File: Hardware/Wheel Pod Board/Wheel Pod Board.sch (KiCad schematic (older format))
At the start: 33 parts, among them J1 Conn_RJ-45, P1 UIM240XX_Stepper_Conn, P2 RS232, P3 ST_SWD_Connector, P4 SyRen, P5 BATT, U1 STM32F401RCT6, U2 SN75176BDR, U3 ZXCT1107, U4 ZXCT1107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

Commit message: Change header footprints to new ones in schematic
Forgot to save this until now, did this before I made the PCB changes
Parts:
- P1, P3: footprint MAVRIC_footprints:1x6_SMD_header -> MAVRIC_footprints:1x6_Breakaway_Header
- P2: footprint MAVRIC_footprints:1x3_SMD_header -> MAVRIC_footprints:1x3_Breakaway_Header
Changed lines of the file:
@@
 Connection ~ 6100 1400
 Wire Wire Line
-	5950 1800 6100 1800
-Wire Wire Line
-	6100 1800 6800 1800
+	5950 1800 6800 1800
 Connection ~ 6100 1800
 Wire Wire Line
@@
 Connection ~ 6600 1100
 Wire Wire Line
-	6100 1200 6100 1400
-Wire Wire Line
-	6100 1400 6100 1600
-Wire Wire Line
-	6100 1600 6100 1800
-Wire Wire Line
-	6600 1000 6600 1100
-Wire Wire Line
-	6600 1100 6600 1300
-Wire Wire Line
-	6600 1300 6600 1500
-Wire Wire Line
-	6600 1500 6600 1700
-Wire Wire Line
-	6600 1700 6600 1900
+	6100 1200 6100 1800
+Wire Wire Line
+	6600 1000 6600 1900
 Wire Wire Line
 	5950 2600 6100 2600
@@
 	2350 7100 2500 7100
 Wire Wire Line
-	1750 7000 2350 7000
-Wire Wire Line
-	2350 7000 2500 7000
+	1750 7000 2500 7000
 Wire Wire Line
 	2500 7200 2350 7200
@@
 	9900 1650 9900 1750
 Wire Wire Line
-	7500 1500 7500 1650
-Wire Wire Line
-	7500 1650 7500 1750
+	7500 1500 7500 1750
 Connection ~ 7500 1650
 Wire Wire Line
@@
 Connection ~ 9900 2350
 Wire Wire Line
-	10400 1550 10400 1650
-Wire Wire Line
-	10400 1650 10400 1750
+	10400 1550 10400 1750
 Connection ~ 9900 1650
 Connection ~ 10400 1650
@@
 	10800 1650 10800 1750
 Wire Wire Line
-	10800 2250 10800 2350
-Wire Wire Line
-	10800 2350 10800 2450
+	10800 2250 10800 2450
 Wire Wire Line
 	10400 2350 10400 2250
@@
 	10400 1650 10800 1650
 Wire Wire Line
-	7500 2350 7900 2350
-Wire Wire Line
-	7900 2350 8300 2350
-Wire Wire Line
-	8300 2350 8700 2350
-Wire Wire Line
-	8700 2350 9100 2350
-Wire Wire Line
-	9100 2350 9500 2350
-Wire Wire Line
-	9500 2350 9900 2350
-Wire Wire Line
-	9900 2350 10400 2350
-Wire Wire Line
-	10400 2350 10800 2350
-Wire Wire Line
-	7350 1650 7500 1650
-Wire Wire Line
-	7500 1650 7900 1650
-Wire Wire Line
-	7900 1650 8300 1650
-Wire Wire Line
-	8300 1650 8700 1650
-Wire Wire Line
-	8700 1650 9100 1650
-Wire Wire Line
-	9100 1650 9500 1650
-Wire Wire Line
-	9500 1650 9900 1650
+	7500 2350 10800 2350
+Wire Wire Line
+	7350 1650 9900 1650
 Wire Wire Line
 	7350 1500 7350 1650
@@
 F 0 "P3" H 9200 6300 50  0000 C CNN
 F 1 "ST_SWD_Connector" H 9200 5600 50  0000 C CNN
-F 2 "MAVRIC_footprints:1x6_SMD_header" H 9200 5950 60  0001 C CNN
+F 2 "MAVRIC_footprints:1x6_Breakaway_Header" H 9200 5950 60  0001 C CNN
 F 3 "" H 9200 5950 60  0000 C CNN
 	1    9200 5950
@@
 OSC_OUT
 Wire Wire Line
-	3950 1500 3950 1800
-Wire Wire Line
-	3950 1800 3950 1950
+	3950 1500 3950 1950
 Wire Wire Line
 	3950 1800 4100 1800
@@
 	4600 1800 4750 1800
 Wire Wire Line
-	4750 1500 4750 1800
-Wire Wire Line
-	4750 1800 4750 1950
+	4750 1500 4750 1950
 Wire Wire Line
 	3950 2450 3950 2600
 Wire Wire Line
-	3950 2600 4350 2600
-Wire Wire Line
-	4350 2600 4750 2600
+	3950 2600 4750 2600
 Wire Wire Line
 	4750 2600 4750 2450
@@
 F 0 "P1" H 7950 6250 50  0000 C CNN
 F 1 "UIM240XX_Stepper_Conn" H 7550 5550 50  0000 C CNN
-F 2 "MAVRIC_footprints:1x6_SMD_header" H 7950 5900 60  0001 C CNN
+F 2 "MAVRIC_footprints:1x6_Breakaway_Header" H 7950 5900 60  0001 C CNN
 F 3 "" H 7950 5900 60  0000 C CNN
 	1    7950 5900
@@
 	7450 4050 7450 4250
 Wire Wire Line
-	6450 4350 6550 4350
-Wire Wire Line
-	6550 4350 6800 4350
+	6450 4350 6800 4350
 Wire Wire Line
 	6550 4450 6550 4350
@@
 	7850 3900 7800 3900
 Wire Wire Line
-	7250 3600 7250 3900
-Wire Wire Line
-	7250 3900 7250 4050
+	7250 3600 7250 4050
 Wire Wire Line
 	7300 3900 7250 3900
@@
 $EndComp
 Wire Wire Line
-	4350 7300 4650 7300
-Wire Wire Line
-	4650 7300 5000 7300
+	4350 7300 5000 7300
 $Comp
 L PWR_FLAG #FLG011
@@
 $EndComp
 Wire Wire Line
-	7850 3850 7850 3900
-Wire Wire Line
-	7850 3900 7850 4050
+	7850 3850 7850 4050
 Wire Wire Line
 	6550 4950 6550 5050
@@
 StepperCurrent
 Wire Wire Line
-	6900 3600 7050 3600
-Wire Wire Line
-	7050 3600 7250 3600
-Wire Wire Line
-	7250 3600 9150 3600
-Wire Wire Line
-	9150 3600 10700 3600
+	6900 3600 10700 3600
 $Comp
 L ZXCT1107 U4
@@
 	9350 4050 9350 4250
 Wire Wire Line
-	8350 4350 8450 4350
-Wire Wire Line
-	8450 4350 8700 4350
+	8350 4350 8700 4350
 Wire Wire Line
 	8450 4450 8450 4350
@@
 	9750 3900 9700 3900
 Wire Wire Line
-	9150 3600 9150 3900
-Wire Wire Line
-	9150 3900 9150 4050
+	9150 3600 9150 4050
 Wire Wire Line
 	9200 3900 9150 3900
@@
 SyRenCurrent
 Wire Wire Line
-	6900 3500 7050 3500
-Wire Wire Line
-	7050 3500 9750 3500
-Wire Wire Line
-	9750 3500 10950 3500
+	6900 3500 10950 3500
 Wire Wire Line
 	10950 3500 10950 3800
@@
 Connection ~ 7250 3600
 Wire Wire Line
-	9750 3850 9750 3900
-Wire Wire Line
-	9750 3900 9750 4050
+	9750 3850 9750 4050
 Wire Wire Line
 	9750 3850 9950 3850
@@
 F 0 "P2" H 10800 6150 50  0000 C CNN
 F 1 "RS232" H 10800 5750 50  0000 C CNN
-F 2 "MAVRIC_footprints:1x3_SMD_header" H 10800 5950 60  0001 C CNN
+F 2 "MAVRIC_footprints:1x3_Breakaway_Header" H 10800 5950 60  0001 C CNN
 F 3 "" H 10800 5950 60  0000 C CNN
 	1    10800 5950
@@
 	3550 7000 3550 6800
 Wire Wire Line
-	3550 6800 4000 6800
-Wire Wire Line
-	4000 6800 4200 6800
+	3550 6800 4200 6800
 Wire Wire Line
 	4200 6800 4200 7000
@@
 	3550 7100 3550 7300
 Wire Wire Line
-	3550 7300 4000 7300
-Wire Wire Line
-	4000 7300 4200 7300
+	3550 7300 4200 7300
 Wire Wire Line
 	4200 7300 4200 7100
@@
 Connection ~ 4650 7300
 Wire Wire Line
-	4400 6900 4650 6900
-Wire Wire Line
-	4650 6900 5000 6900
+	4400 6900 5000 6900
 $Comp
 L PWR_FLAG #FLG023
@@
 	5000 7200 4850 7200
 Wire Wire Line
-	4850 7200 4850 7400
-Wire Wire Line
-	4850 7400 4850 7500
+	4850 7200 4850 7500
 Wire Wire Line
 	5000 7400 4850 7400

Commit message: Add pads for connecting encoder
Schematic, PCB, and in cube
Resolves #16
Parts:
- added J2: M3 Encoder, Wire_Pads:SolderWirePad_3x_0-8mmDrill, symbol Conn-3
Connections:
- net +5V: now also J2.1
- net GND: now also J2.3
- net at U1.55 (PB3): now also J2.2
- no-connect marks 38 -> 37
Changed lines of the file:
@@
 NoConn ~ 1650 3100
 NoConn ~ 1650 3200
-NoConn ~ 1650 3300
 NoConn ~ 1650 3400
 NoConn ~ 1650 3500
@@
 Wire Wire Line
 	3050 6050 3150 6050
+$Comp
+L Conn-3 J2
+U 1 1 54FD025C
+P 3000 3300
+F 0 "J2" H 3000 3500 60  0000 C CNN
+F 1 "M3 Encoder" H 3000 3100 60  0000 C CNN
+F 2 "Wire_Pads:SolderWirePad_3x_0-8mmDrill" H 3000 3350 60  0001 C CNN
+F 3 "" H 3000 3350 60  0000 C CNN
+	1    3000 3300
+	-1   0    0    -1
+$EndComp
+Wire Wire Line
+	2700 3400 2600 3400
+Wire Wire Line
+	2600 3400 2600 3500
+$Comp
+L GND #PWR026
+U 1 1 54FD0A9D
+P 2600 3500
+F 0 "#PWR026" H 2600 3250 60  0001 C CNN
+F 1 "GND" H 2600 3350 60  0000 C CNN
+F 2 "" H 2600 3500 60  0000 C CNN
+F 3 "" H 2600 3500 60  0000 C CNN
+	1    2600 3500
+	1    0    0    -1
+$EndComp
+Wire Wire Line
+	2700 3200 2450 3200
+$Comp
+L +5V #PWR027
+U 1 1 54FD0BA4
+P 2450 3200
+F 0 "#PWR027" H 2450 3050 60  0001 C CNN
+F 1 "+5V" H 2450 3340 60  0000 C CNN
+F 2 "" H 2450 3200 60  0000 C CNN
+F 3 "" H 2450 3200 60  0000 C CNN
+	1    2450 3200
+	0    -1   -1   0
+$EndComp
+Wire Wire Line
+	1650 3300 2700 3300
 $EndSCHEMATC

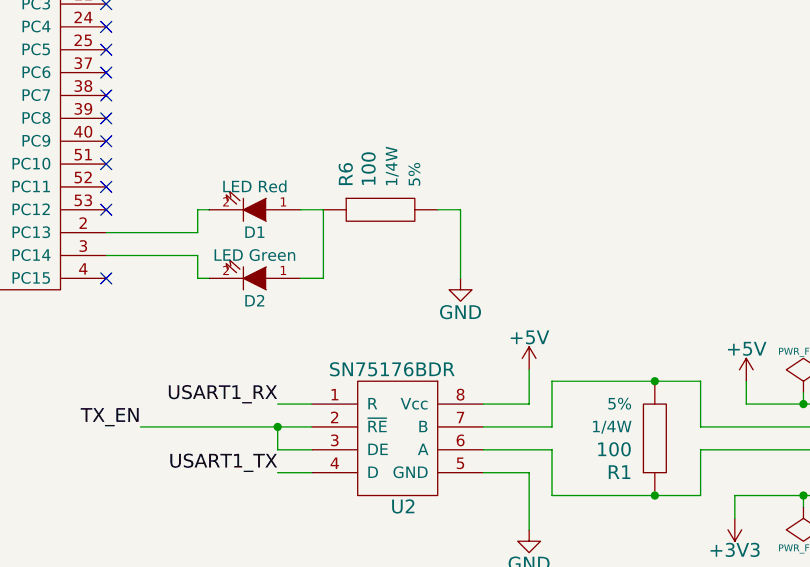
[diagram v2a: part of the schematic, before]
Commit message: Add resistor for green LED, clean up references
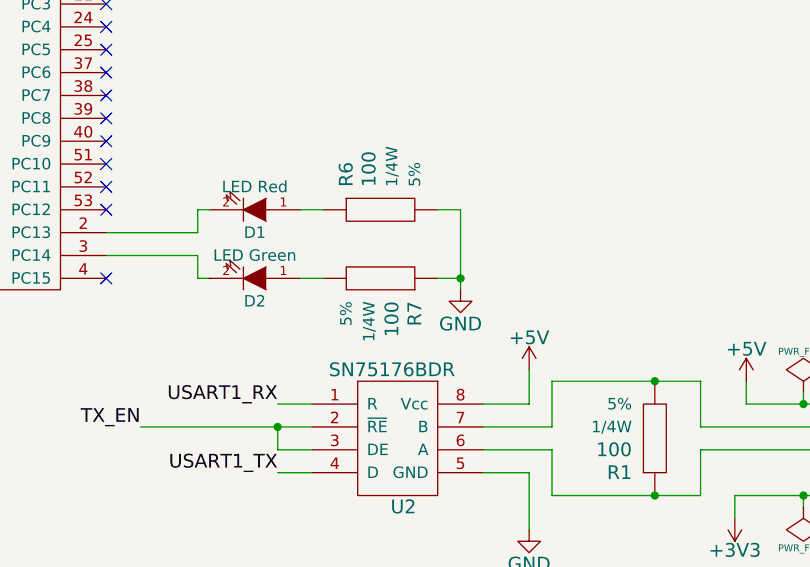
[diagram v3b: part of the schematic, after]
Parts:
- added R7: 100, Resistors_SMD:R_1206_HandSoldering, symbol Resistor
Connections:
- net GND: now also R7.1
- net at D1.1 (A), R6.1: no longer D2.1 (A)
- new net: D2.1 (A), R7.2
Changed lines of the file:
@@
 	2000 6350 2050 6350
 Wire Wire Line
-	3150 6050 3150 6350
+	3150 6050 3150 6400
 $Comp
 L GND #PWR025
 U 1 1 54FBE69D
-P 3150 6350
-F 0 "#PWR025" H 3150 6100 60  0001 C CNN
-F 1 "GND" H 3150 6200 60  0000 C CNN
-F 2 "" H 3150 6350 60  0000 C CNN
-F 3 "" H 3150 6350 60  0000 C CNN
-	1    3150 6350
+P 3150 6400
+F 0 "#PWR025" H 3150 6150 60  0001 C CNN
+F 1 "GND" H 3150 6250 60  0000 C CNN
+F 2 "" H 3150 6400 60  0000 C CNN
+F 3 "" H 3150 6400 60  0000 C CNN
+	1    3150 6400
 	1    0    0    -1
 $EndComp
@@
 Wire Wire Line
 	2450 6350 2550 6350
-Wire Wire Line
-	2550 6350 2550 6050
 Wire Wire Line
 	2550 6050 2450 6050
@@
 Wire Wire Line
 	1650 3300 2700 3300
+$Comp
+L Resistor R7
+U 1 1 54FD7A02
+P 2800 6350
+F 0 "R7" V 2650 6450 60  0000 L CNN
+F 1 "100" V 2750 6450 60  0000 L CNN
+F 2 "Resistors_SMD:R_1206_HandSoldering" H 2700 6350 60  0001 C CNN
+F 3 "" H 2800 6450 60  0001 C CNN
+F 4 "Panasonic" H 2800 6350 60  0001 C CNN "Manufacturer"
+F 5 "ERJ-8GEYJ101V" H 2800 6350 60  0001 C CNN "Manufacturer Part #"
+F 6 "Digi-Key" H 2800 6350 60  0001 C CNN "Vendor"
+F 7 "P100ECT-ND" H 2800 6350 60  0001 C CNN "Vendor Part #"
+F 8 "1/4W" V 2850 6450 50  0000 L CNN "Power"
+F 9 "5%" V 2950 6450 50  0000 L CNN "Tolerance"
+	1    2800 6350
+	-1   0    0    1
+$EndComp
+Wire Wire Line
+	3150 6350 3050 6350
+Connection ~ 3150 6350
 $EndSCHEMATC

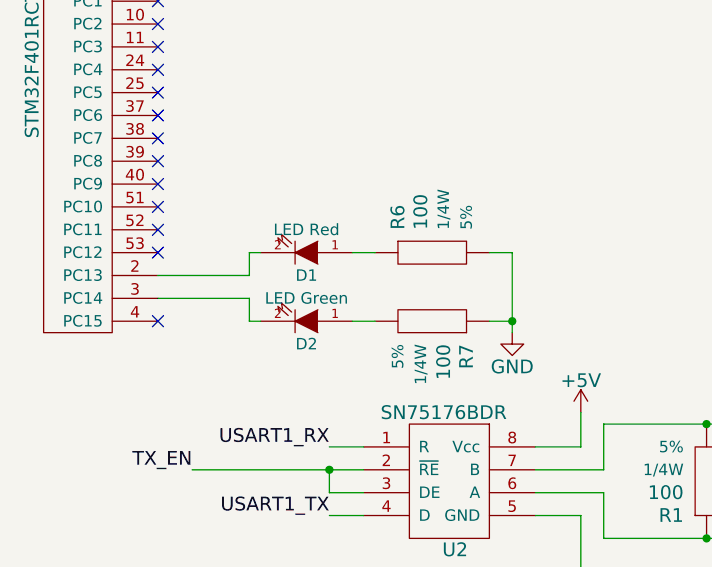
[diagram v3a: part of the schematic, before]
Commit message: Fix LED polarity
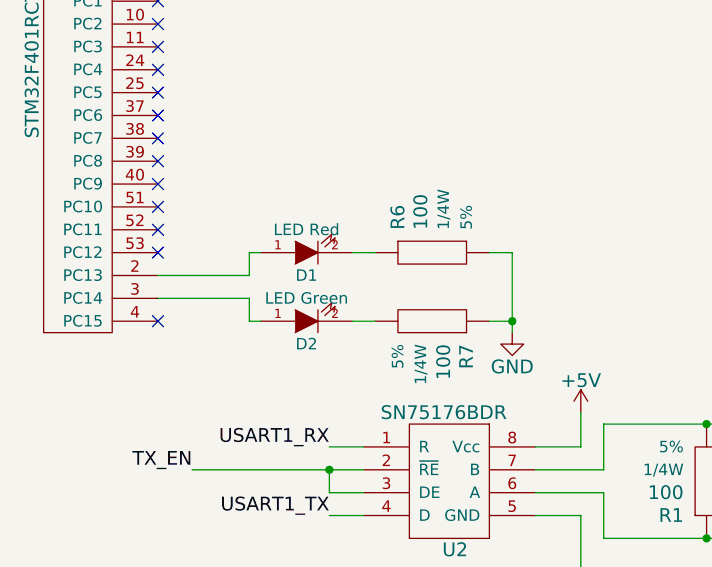
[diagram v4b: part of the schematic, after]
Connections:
- net at U1.2 (PC13): now also D1.1 (A); no longer D1.2 (K)
- net at U1.3 (PC14): now also D2.1 (A); no longer D2.2 (K)
- net at R6.1: now also D1.2 (K); no longer D1.1 (A)
- net at R7.2: now also D2.2 (K); no longer D2.1 (A)
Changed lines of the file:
@@
 F 5 "475-1415-1-ND" H 2250 6050 60  0001 C CNN "Vendor Part #"
 	1    2250 6050
-	-1   0    0    1
+	1    0    0    1
 $EndComp
 $Comp
@@
 F 5 "475-1410-1-ND" H 2250 6350 60  0001 C CNN "Vendor Part #"
 	1    2250 6350
-	-1   0    0    1
+	1    0    0    1
 $EndComp
 Wire Wire Line
